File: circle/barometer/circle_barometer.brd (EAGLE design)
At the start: 10 x 10 mm, 8 parts

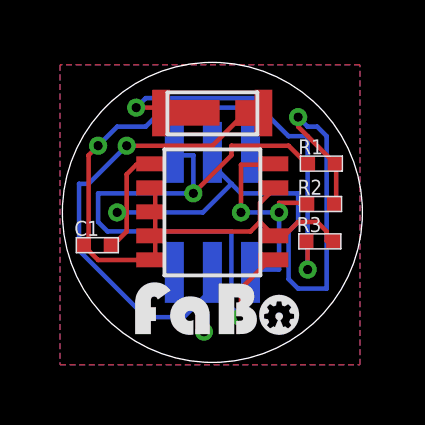
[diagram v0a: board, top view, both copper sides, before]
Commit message: Add barometer
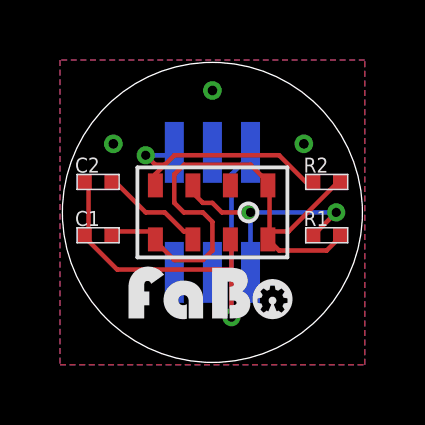
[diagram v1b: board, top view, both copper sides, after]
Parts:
- removed LED1: NSSW157T, FaBo-LED:NSSW157T
- removed R3: (no value), FaBo-Resistors:0402
- removed S1: HAMAMATSU-S11059, gclueSensor:HAMAMATSU-S11059
- added C2: 1uF, FaBo-Capacitor:0402
- added U$3: (no value), FaBo:LOGO_FABO_S
- C1: value 0.1uf -> 1uF
- U$2: value (none) -> I2C-MPL115A2; device FaBo:LOGO_FABO_S -> gclue:I2C-MLP115A2
- moved U$2 4.09 mm to (5.08, 5.08), turned to 90 degrees
- moved R1 2.39 mm to (8.89, 4.32)
- moved R2 0.76 mm to (8.89, 6.10)
- moved C1 0.33 mm to (1.27, 4.32)
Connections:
- removed net +3V3: C1.P$2, R1.P$2, R2.P$2, S1.1, U$4.VCC
- removed net N$2: LED1.CATHODE1, LED1.CATHODE2, R3.P$1
- new net VCC: C1.P$2, R1.P$2, R2.P$2, U$2.RST, U$2.SHDN, U$2.VDD
- net GND: now also C2.P$1, U$2.GND; no longer R3.P$2, S1.2, S1.3, S1.4, S1.5, S1.7, S1.8
- net N$1: now also C2.P$2, U$2.CAP; no longer LED1.ANODE1, LED1.ANODE2, U$4.2
- net SCL: now also R2.P$1, U$2.SCL; no longer R1.P$1, S1.6
- net SDA: now also R1.P$1, U$2.SDA; no longer R2.P$1, S1.9
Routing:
- net +3V3: track 25.9 -> 0.00 mm, vias 2 -> 0
- net VCC: track 0.00 -> 18.8 mm
- net N$2: track 14.3 -> 0.00 mm, vias 2 -> 0
- net SCL: track 21.1 -> 8.11 mm, vias 2 -> 1
- net N$1: track 15.8 -> 3.65 mm, vias 1 -> 0
- net GND: track 24.3 -> 15.7 mm, vias 2 -> 4
